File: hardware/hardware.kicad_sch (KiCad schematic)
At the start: 59 parts, among them J1 SMA, J2 Test Header, P5 BMIS-202-C, U1 CC1101, U2 CC1190, U3 B39921B3588U410, X1 26.000 MHz

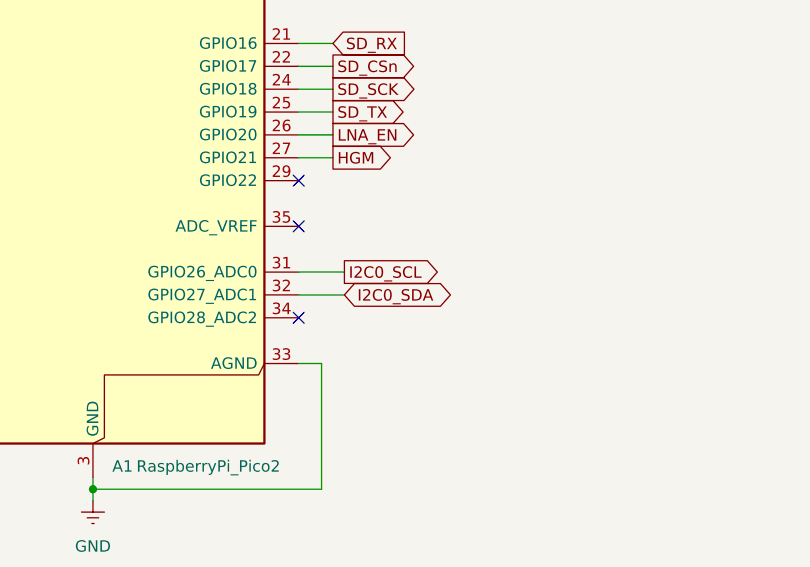
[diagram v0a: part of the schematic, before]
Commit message: Fixed I2C1 global labels.
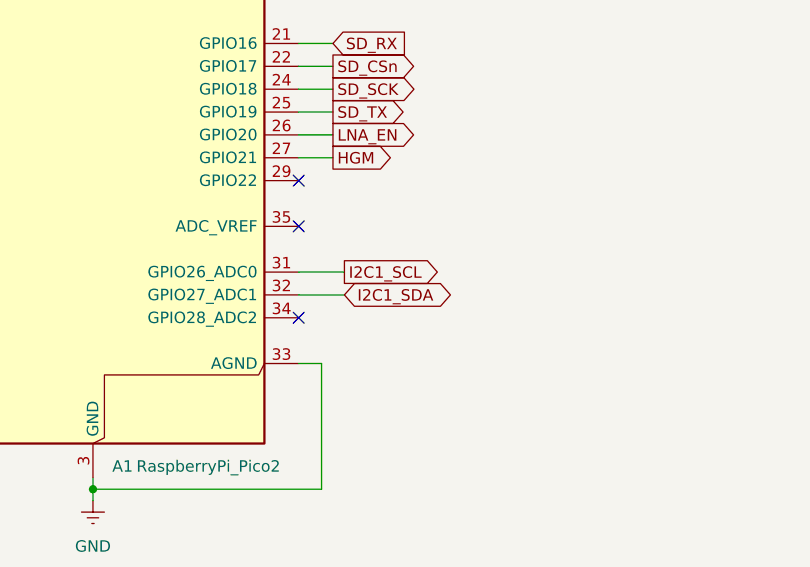
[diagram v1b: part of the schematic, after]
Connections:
- net I2C0_SCL: no longer A1.31 (GPIO26_ADC0)
- net I2C0_SDA: no longer A1.32 (GPIO27_ADC1)
- new net I2C1_SCL: A1.31 (GPIO26_ADC0)
- new net I2C1_SDA: A1.32 (GPIO27_ADC1)
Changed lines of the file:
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@@
 		)
 	)
-	(global_label "I2C0_SCL"
+	(global_label "I2C1_SCL"
 		(shape output)
 		(at 87.63 72.39 0)
@@
 		)
 	)
-	(global_label "I2C0_SDA"
+	(global_label "I2C1_SDA"
 		(shape bidirectional)
 		(at 87.63 74.93 0)

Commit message: Worked on PCB routing and component placement.
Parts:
- added R3, R4, R5: 10K, Resistor_SMD:R_0603_1608Metric, symbol Device:R_US
- A1: Digikey Link (none) -> https://www.digikey.com/en/products/detail/raspberry-pi/SC1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; Digikey Part Number (none) -> 2648-SC1631CT-ND
- D1: Digikey Link (none) -> https://www.digikey.com/en/products/detail/w%C3%BCrth-elekt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; Digikey Part Number (none) -> 732-5016-ND
- D2: Digikey Link (none) -> https://www.digikey.com/en/products/detail/w%C3%BCrth-elekt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; Digikey Part Number (none) -> 732-5015-ND
- FB1: Digikey Link (none) -> https://www.digikey.com/en/products/detail/laird-signal-int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; Digikey Part Number (none) -> 240-2397-1-ND
- P5: value BMIS-202-C -> BMI-S-205-C; footprint RF_Shielding:Laird_Technologies_BMI-S-202-F_16.50x16.50mm -> RF_Shielding:Laird_Technologies_BMI-S-203-F_26.21x26.21mm; Digikey Link (none) -> https://www.digikey.com/en/products/detail/laird-technologi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; Digikey Part Number (none) -> 903-1014-ND
- R1, R2: footprint Resistor_SMD:R_1206_3216Metric -> Resistor_SMD:R_0603_1608Metric; Digikey Link (none) -> https://www.digikey.com/en/products/detail/vishay/MCT06030C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; Digikey Part Number (none) -> MCT06030C3300FP500
- R141: footprint Resistor_SMD:R_1206_3216Metric -> Resistor_SMD:R_0603_1608Metric; Digikey Link (none) -> https://www.digikey.com/en/products/detail/vishay/MCT06030C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; Digikey Part Number (none) -> MCT0603-3.30K-CFCT-ND
- R151: footprint Resistor_SMD:R_1206_3216Metric -> Resistor_SMD:R_0603_1608Metric; Digikey Link (none) -> https://www.digikey.com/en/products/detail/vishay/MCT06030C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; Digikey Part Number (none) -> MCT0603-47.0-CFCT-ND
- R161: footprint Resistor_SMD:R_1206_3216Metric -> Resistor_SMD:R_0603_1608Metric; Digikey Link (none) -> https://www.digikey.com/en/products/detail/vishay/MCT06030C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; Digikey Part Number (none) -> MCT0603-10.0-CFCT-ND
- R171: footprint Resistor_SMD:R_1206_3216Metric -> Resistor_SMD:R_0603_1608Metric; Digikey Link (none) -> https://www.digikey.com/en/products/detail/vishay/MCT06030C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; Digikey Part Number (none) -> 749-1667-1-ND
- TP1, TP2: Digikey Part Number (none) -> JSTXH
- U1: Digikey Link (none) -> https://www.digikey.com/en/products/detail/texas-instrument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; Digikey Part Number (none) -> 296-35718-1-ND
- U2: Digikey Link (none) -> https://www.digikey.com/en/products/detail/texas-instrument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; Digikey Part Number (none) -> 296-36922-1-ND
- U3: Digikey Link (none) -> https://www.digikey.com/en/products/detail/qualcomm-rf-fron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; Digikey Part Number (none) -> 495-1674-1-ND
- X1: footprint Crystal:Crystal_SMD_3225-4Pin_3.2x2.5mm -> Crystal:Crystal_SMD_2016-4Pin_2.0x1.6mm; Digikey Link (none) -> https://www.digikey.com/en/products/detail/kyocera-avx/CX20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; Digikey Part Number (none) -> 478-CX2016FB26000F0FZZH1CT-ND
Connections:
- net HGM: now also R3.2; no longer U2.6 (HGM)
- net LNA_EN: now also R4.2; no longer U2.7 (LNA_EN)
- net PA_EN: now also R5.2; no longer U2.8 (PA_EN)
- new net: R3.1, U2.6 (HGM)
- new net: R4.1, U2.7 (LNA_EN)
- new net: R5.1, U2.8 (PA_EN)
